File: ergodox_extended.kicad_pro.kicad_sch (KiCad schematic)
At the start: 119 parts, among them J1 USB_B_Micro, J2 AudioJack4, J3 AudioJack4, J4 ISP, SW0:0 SWITCH, SW0:1 SWITCH, SW0:2 SWITCH, SW0:3 SWITCH, SW0:4 SWITCH, SW0:5 SWITCH, SW0:6 SWITCH, SW1 Reset, SW1:0 SWITCH, SW1:1 SWITCH, SW1:2 SWITCH, SW1:3 SWITCH, SW1:4 SWITCH, SW1:5 SWITCH, SW1:6 SWITCH, SW2:0 SWITCH, SW2:1 SWITCH, SW2:2 SWITCH, SW2:3 SWITCH, SW2:4 SWITCH, SW2:5 SWITCH, SW2:6 SWITCH, SW3:0 SWITCH, SW3:1 SWITCH, SW3:2 SWITCH, SW3:3 SWITCH, SW3:4 SWITCH, SW3:5 SWITCH, SW3:6 SWITCH, SW4:0 SWITCH, SW4:1 SWITCH, SW4:2 SWITCH, SW4:3 SWITCH, SW4:4 SWITCH, SW4:5 SWITCH, SW4:6 SWITCH, SW5:0 SWITCH, SW5:1 SWITCH, SW5:2 SWITCH, SW5:3 SWITCH, SW5:4 SWITCH, SW5:5 SWITCH, SW5:6 SWITCH, SW6:0 SWITCH, SW6:1 SWITCH, SW6:2 SWITCH, SW6:3 SWITCH, SW6:4 SWITCH, SW6:5 SWITCH, SW6:6 SWITCH, U1 ATmega32U4-AU, U2 MCP23018-E_SS, Y1 16Mhz

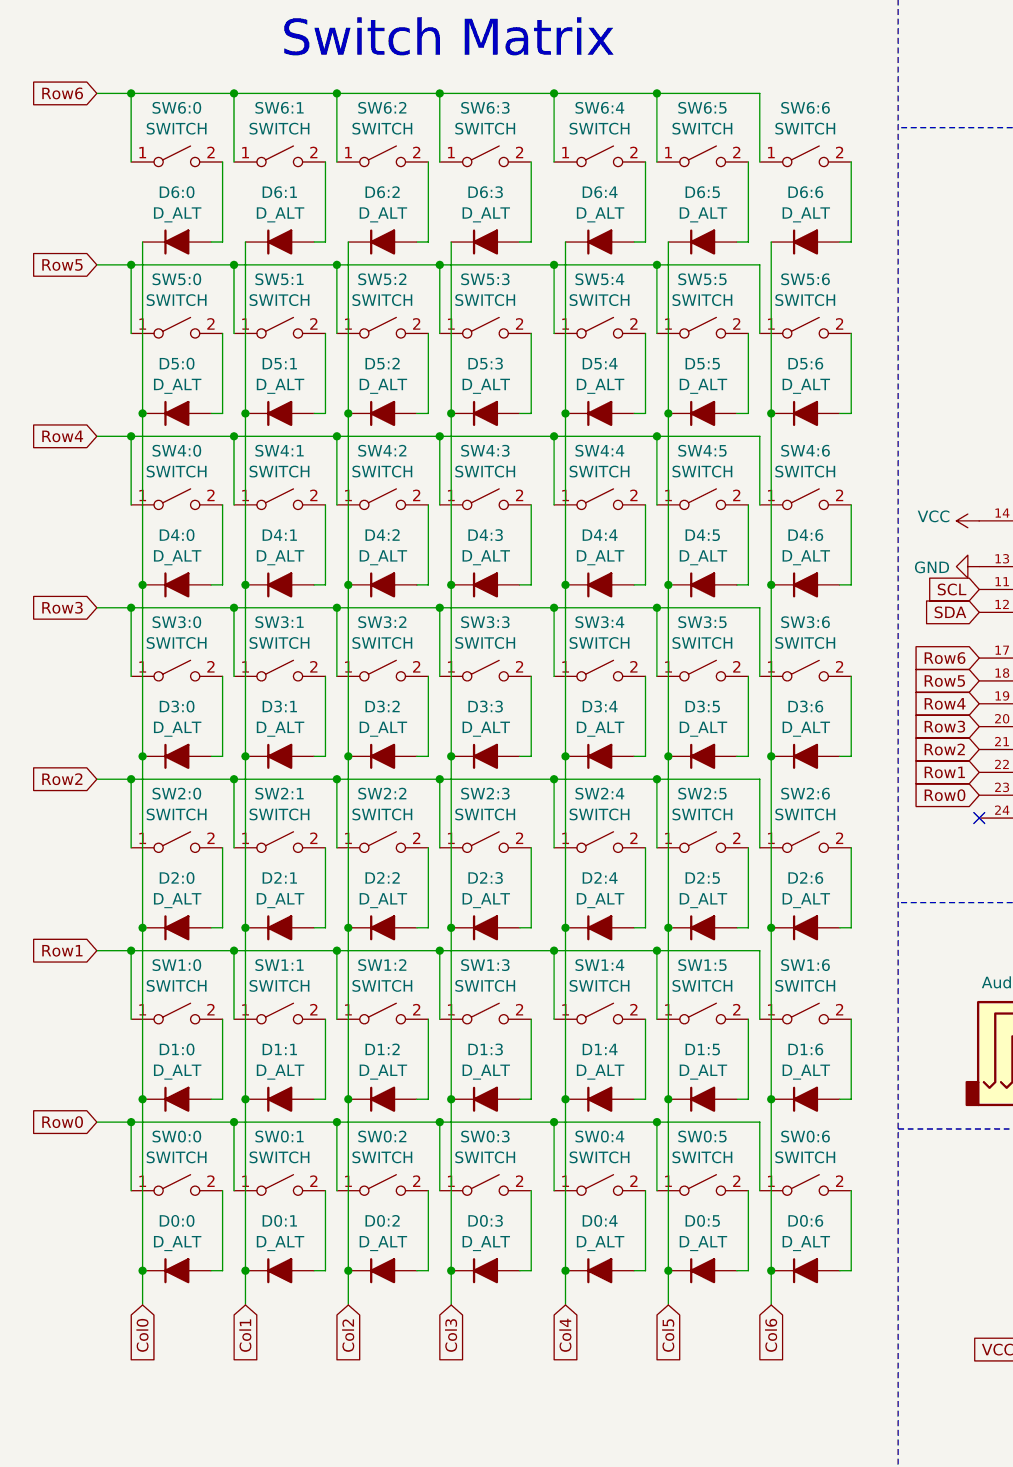
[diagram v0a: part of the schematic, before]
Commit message: Fix diode dir, write readme
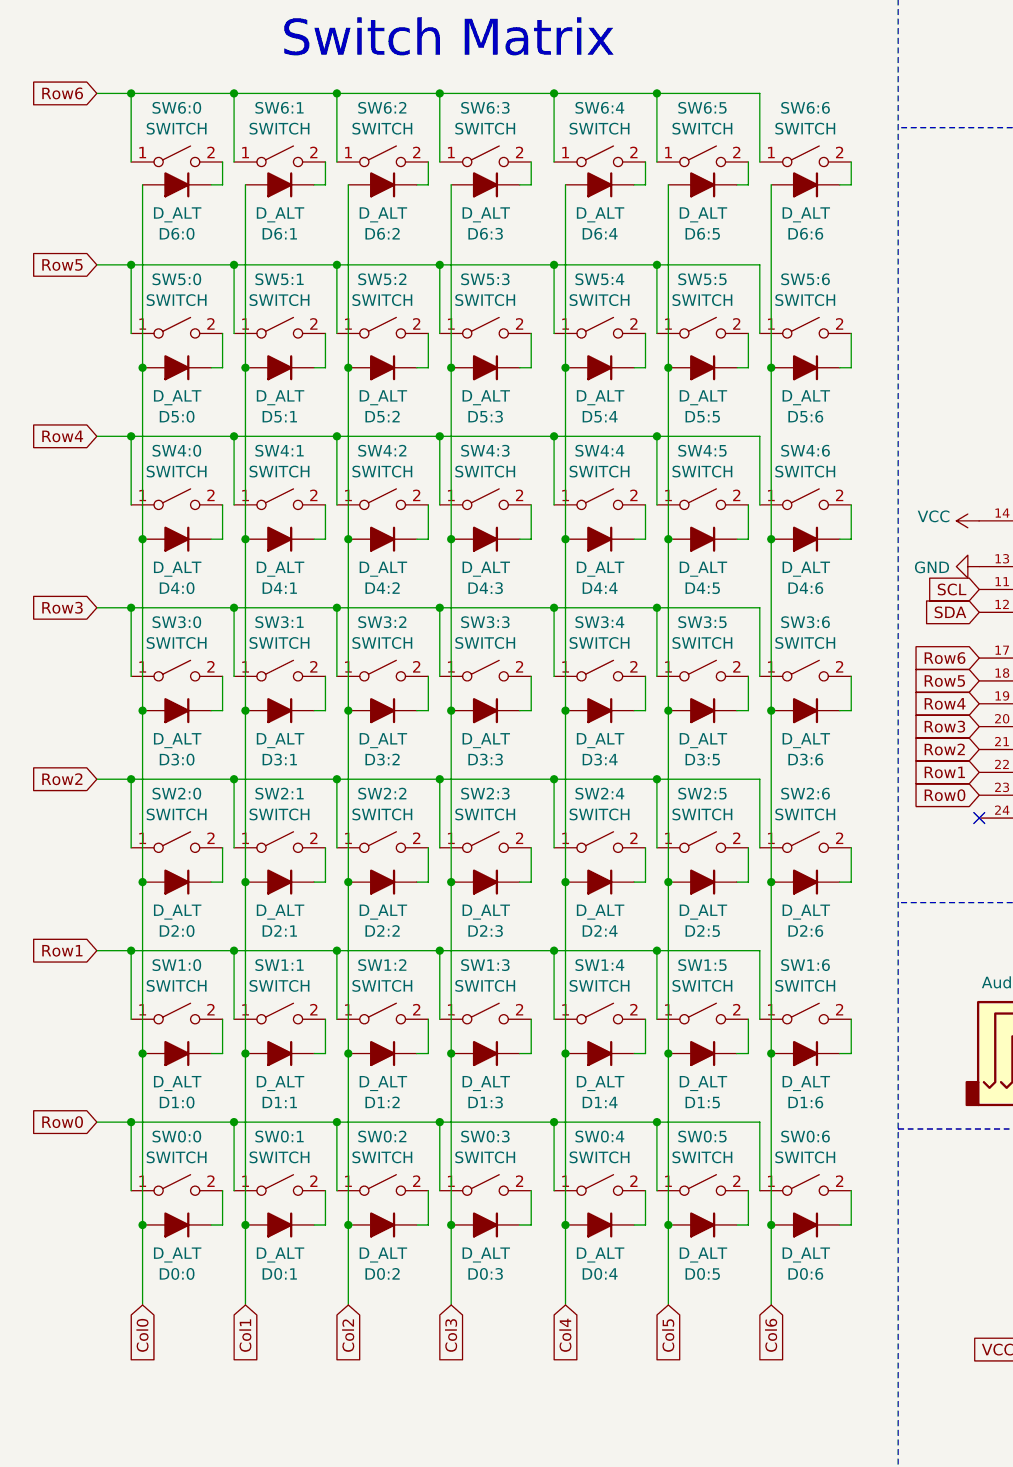
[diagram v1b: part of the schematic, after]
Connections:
- net Col0: now also D0:0.2 (A), D1:0.2 (A), D2:0.2 (A), D3:0.2 (A), D4:0.2 (A), D5:0.2 (A), D6:0.2 (A); no longer D0:0.1 (K), D1:0.1 (K), D2:0.1 (K), D3:0.1 (K), D4:0.1 (K), D5:0.1 (K), D6:0.1 (K)
- net Col1: now also D0:1.2 (A), D1:1.2 (A), D2:1.2 (A), D3:1.2 (A), D4:1.2 (A), D5:1.2 (A), D6:1.2 (A); no longer D0:1.1 (K), D1:1.1 (K), D2:1.1 (K), D3:1.1 (K), D4:1.1 (K), D5:1.1 (K), D6:1.1 (K)
- net Col2: now also D0:2.2 (A), D1:2.2 (A), D2:2.2 (A), D3:2.2 (A), D4:2.2 (A), D5:2.2 (A), D6:2.2 (A); no longer D0:2.1 (K), D1:2.1 (K), D2:2.1 (K), D3:2.1 (K), D4:2.1 (K), D5:2.1 (K), D6:2.1 (K)
- net Col3: now also D0:3.2 (A), D1:3.2 (A), D2:3.2 (A), D3:3.2 (A), D4:3.2 (A), D5:3.2 (A), D6:3.2 (A); no longer D0:3.1 (K), D1:3.1 (K), D2:3.1 (K), D3:3.1 (K), D4:3.1 (K), D5:3.1 (K), D6:3.1 (K)
- net Col4: now also D0:4.2 (A), D1:4.2 (A), D2:4.2 (A), D3:4.2 (A), D4:4.2 (A), D5:4.2 (A), D6:4.2 (A); no longer D0:4.1 (K), D1:4.1 (K), D2:4.1 (K), D3:4.1 (K), D4:4.1 (K), D5:4.1 (K), D6:4.1 (K)
- net Col5: now also D0:5.2 (A), D1:5.2 (A), D2:5.2 (A), D3:5.2 (A), D4:5.2 (A), D5:5.2 (A), D6:5.2 (A); no longer D0:5.1 (K), D1:5.1 (K), D2:5.1 (K), D3:5.1 (K), D4:5.1 (K), D5:5.1 (K), D6:5.1 (K)
- net Col6: now also D0:6.2 (A), D1:6.2 (A), D2:6.2 (A), D3:6.2 (A), D4:6.2 (A), D5:6.2 (A), D6:6.2 (A); no longer D0:6.1 (K), D1:6.1 (K), D2:6.1 (K), D3:6.1 (K), D4:6.1 (K), D5:6.1 (K), D6:6.1 (K)
- net at SW6:0.2 (B): now also D6:0.1 (K); no longer D6:0.2 (A)
- net at SW6:1.2 (B): now also D6:1.1 (K); no longer D6:1.2 (A)
- net at SW6:2.2 (B): now also D6:2.1 (K); no longer D6:2.2 (A)
- net at SW6:3.2 (B): now also D6:3.1 (K); no longer D6:3.2 (A)
- net at SW6:4.2 (B): now also D6:4.1 (K); no longer D6:4.2 (A)
- net at SW6:5.2 (B): now also D6:5.1 (K); no longer D6:5.2 (A)
- net at SW6:6.2 (B): now also D6:6.1 (K); no longer D6:6.2 (A)
- net at SW5:0.2 (B): now also D5:0.1 (K); no longer D5:0.2 (A)
- net at SW5:1.2 (B): now also D5:1.1 (K); no longer D5:1.2 (A)
- net at SW5:2.2 (B): now also D5:2.1 (K); no longer D5:2.2 (A)
- net at SW5:3.2 (B): now also D5:3.1 (K); no longer D5:3.2 (A)
- net at SW5:4.2 (B): now also D5:4.1 (K); no longer D5:4.2 (A)
- net at SW5:5.2 (B): now also D5:5.1 (K); no longer D5:5.2 (A)
- net at SW5:6.2 (B): now also D5:6.1 (K); no longer D5:6.2 (A)
- net at SW4:0.2 (B): now also D4:0.1 (K); no longer D4:0.2 (A)
- net at SW4:1.2 (B): now also D4:1.1 (K); no longer D4:1.2 (A)
- net at SW4:2.2 (B): now also D4:2.1 (K); no longer D4:2.2 (A)
- net at SW4:3.2 (B): now also D4:3.1 (K); no longer D4:3.2 (A)
- net at SW4:4.2 (B): now also D4:4.1 (K); no longer D4:4.2 (A)
- net at SW4:5.2 (B): now also D4:5.1 (K); no longer D4:5.2 (A)
- net at SW4:6.2 (B): now also D4:6.1 (K); no longer D4:6.2 (A)
- net at SW3:0.2 (B): now also D3:0.1 (K); no longer D3:0.2 (A)
- net at SW3:1.2 (B): now also D3:1.1 (K); no longer D3:1.2 (A)
- net at SW3:2.2 (B): now also D3:2.1 (K); no longer D3:2.2 (A)
- net at SW3:3.2 (B): now also D3:3.1 (K); no longer D3:3.2 (A)
- net at SW3:4.2 (B): now also D3:4.1 (K); no longer D3:4.2 (A)
- net at SW3:5.2 (B): now also D3:5.1 (K); no longer D3:5.2 (A)
- net at SW3:6.2 (B): now also D3:6.1 (K); no longer D3:6.2 (A)
- net at SW2:0.2 (B): now also D2:0.1 (K); no longer D2:0.2 (A)
- net at SW2:1.2 (B): now also D2:1.1 (K); no longer D2:1.2 (A)
- net at SW2:2.2 (B): now also D2:2.1 (K); no longer D2:2.2 (A)
- net at SW2:3.2 (B): now also D2:3.1 (K); no longer D2:3.2 (A)
- net at SW2:4.2 (B): now also D2:4.1 (K); no longer D2:4.2 (A)
- net at SW2:5.2 (B): now also D2:5.1 (K); no longer D2:5.2 (A)
- net at SW2:6.2 (B): now also D2:6.1 (K); no longer D2:6.2 (A)
- net at SW1:0.2 (B): now also D1:0.1 (K); no longer D1:0.2 (A)
- net at SW1:1.2 (B): now also D1:1.1 (K); no longer D1:1.2 (A)
- net at SW1:2.2 (B): now also D1:2.1 (K); no longer D1:2.2 (A)
- net at SW1:3.2 (B): now also D1:3.1 (K); no longer D1:3.2 (A)
- net at SW1:4.2 (B): now also D1:4.1 (K); no longer D1:4.2 (A)
- net at SW1:5.2 (B): now also D1:5.1 (K); no longer D1:5.2 (A)
- net at SW1:6.2 (B): now also D1:6.1 (K); no longer D1:6.2 (A)
- net at SW0:0.2 (B): now also D0:0.1 (K); no longer D0:0.2 (A)
- net at SW0:1.2 (B): now also D0:1.1 (K); no longer D0:1.2 (A)
- net at SW0:2.2 (B): now also D0:2.1 (K); no longer D0:2.2 (A)
- net at SW0:3.2 (B): now also D0:3.1 (K); no longer D0:3.2 (A)
- net at SW0:4.2 (B): now also D0:4.1 (K); no longer D0:4.2 (A)
- net at SW0:5.2 (B): now also D0:5.1 (K); no longer D0:5.2 (A)
- net at SW0:6.2 (B): now also D0:6.1 (K); no longer D0:6.2 (A)
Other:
- moved on the sheet: D0:0, D0:1, D0:2, D0:3, D0:4, D0:5, D0:6, D1:0, D1:1, D1:2, D1:3, D1:4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
